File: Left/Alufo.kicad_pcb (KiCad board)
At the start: 2 copper layers, 139.7 x 88.9 mm, 73 parts, among them J1 USB_C_Receptacle_USB2.0_16P_2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, J3 USB_C_Receptacle_USB2.0_16P_2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, K11 PG1350, K12 PG1350, K13 PG1350, K14 PG1350, K15 PG1350, K16 PG1350, K21 PG1350, K22 PG1350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

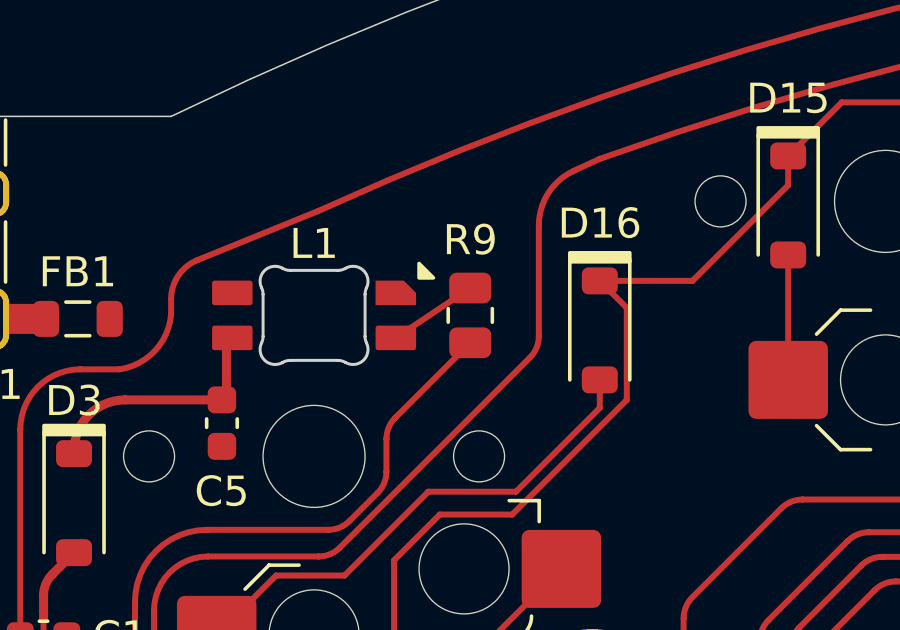
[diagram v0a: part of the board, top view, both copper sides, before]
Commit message: Remove status LED resistor
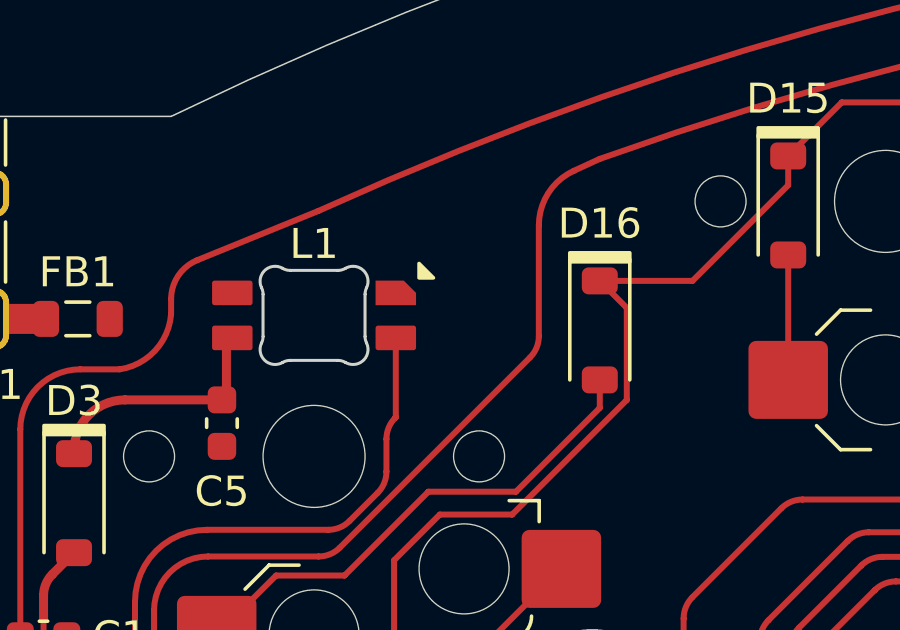
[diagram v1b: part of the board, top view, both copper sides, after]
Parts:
- removed R9: 470R, Resistor_SMD:R_0805_2012Metric
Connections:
- L1 pad 3: Net-(L1-DIN) -> LED
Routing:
- net Net-(L1-DIN): track 2.99 -> 0.00 mm
- net LED: track 25.2 -> 24.3 mm

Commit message: Update logo and add to PCB
Logo now has PCB revision included and is positioned at top left/right edge ±1.25,+1.25mm.
Author is now positioned between lowest row 2 pad 2 and bottom edge, centred to logo.
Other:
- board text added: "${AUTHOR}"
- board text removed: "${PROJECTNAME} v${PCB_REVISION} • ${AUTHOR}"

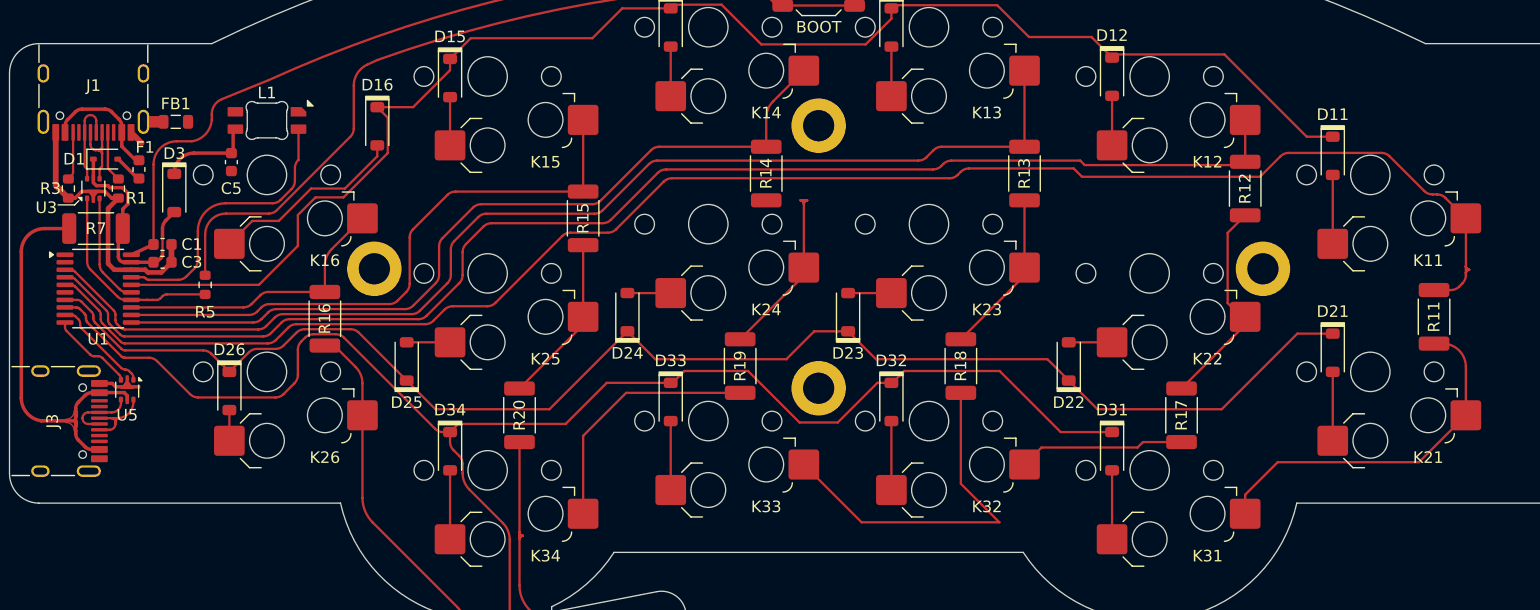
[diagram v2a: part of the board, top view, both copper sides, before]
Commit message: Align upper 0Ω resistors as on righthand, remove R11
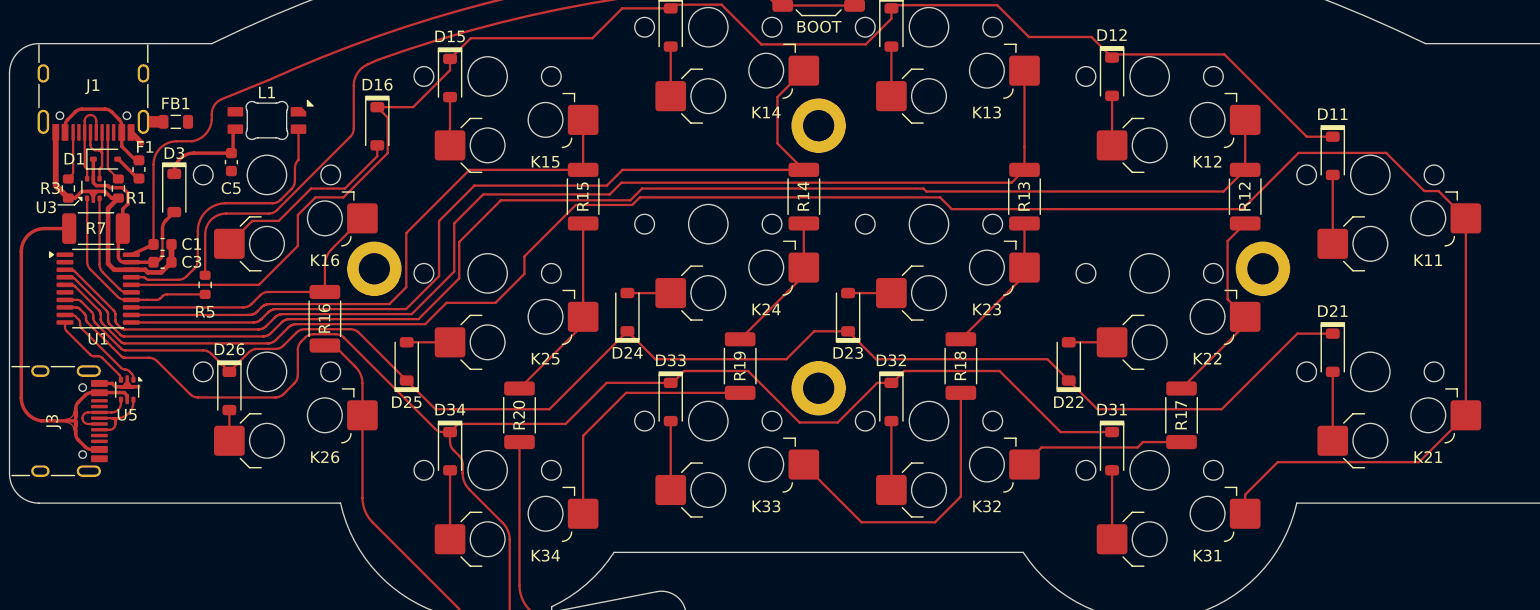
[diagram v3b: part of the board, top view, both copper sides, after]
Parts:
- removed R11: 0R, Project Library:R_2010_5025Metric_Mod
- moved R14 3.81 mm to (151.1, 54.3)
- moved R13 1.99 mm to (170.2, 54.3)
- moved R15 1.88 mm to (132.1, 54.3)
- moved R12 0.70 mm to (189.2, 54.3)
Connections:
- net Col2RT renamed Net-(K32-Pad1)
- net Col3RT renamed Net-(K33-Pad1)
- net Col4RT renamed Net-(K34-Pad1)
- K21 pad 1: Col1T -> Col1
- K31 pad 1: Col1T -> Col1
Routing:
- net Col1: track 139.7 -> 174.2 mm
- net Col1T: track 30.8 -> 0.00 mm
- net Col4L: track 70.5 -> 76.7 mm
- net Net-(K33-Pad1): track 31.5 -> 25.5 mm
- net Col3L: track 99.3 -> 101.5 mm
- net Col3R: track 13.6 -> 11.6 mm
- net Col4R: track 13.6 -> 11.6 mm
- net Col5R: track 14.0 -> 15.8 mm
- net Col2L: track 114.8 -> 116.2 mm
- net Col2R: track 18.1 -> 17.1 mm
- net Col5L: track 52.1 -> 51.2 mm

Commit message: Route Row 2 under upper 0Ω resistors
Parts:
- moved D25 13.7 mm to (127.0, 59.3), turned to -90 degrees
- moved D22 9.98 mm to (177.7, 59.3), turned to -90 degrees
- moved D23 8.47 mm to (158.7, 56.7), turned to -90 degrees
- moved D24 8.47 mm to (139.6, 56.7), turned to -90 degrees
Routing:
- net Net-(D25-A): track 3.74 -> 8.88 mm
- net Net-(D22-A): track 3.74 -> 5.95 mm
- net Row2: track 126.7 -> 128.7 mm
- net Net-(D24-A): track 3.74 -> 4.30 mm
- net Net-(D23-A): track 3.74 -> 4.30 mm
- net Col3L: track 101.5 -> 102.0 mm

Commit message: Route Row 3 under upper 0Ω resistors
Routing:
- net Row3: track 159.5 -> 217.7 mm
- net Row2: track 128.7 -> 129.8 mm
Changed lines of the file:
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@@
 		(net 48)
 	)
+	(gr_poly
+		(pts
+			(arc
+				(start 154.178 54.91)
+				(mid 154.090132 54.697868)
+				(end 153.878 54.61)
+			)
+			(arc
+				(start 154.478 54.61)
+				(mid 154.265868 54.697868)
+				(end 154.178 54.91)
+			)
+		)
+		(stroke
+			(width 0.2)
+			(type solid)
+		)
+		(fill none)
+		(layer "F.Cu")
+		(net 61)
+	)
 	(gr_arc
 		(start 114.3 42.50001)
@@
 		(net 54)
 	)
+	(gr_poly
+		(pts
+			(arc
+				(start 134.874 55.91668)
+				(mid 134.786132 55.704548)
+				(end 134.574 55.61668)
+			)
+			(arc
+				(start 135.174 55.61668)
+				(mid 134.961868 55.704548)
+				(end 134.874 55.91668)
+			)
+		)
+		(stroke
+			(width 0.2)
+			(type solid)
+		)
+		(fill none)
+		(layer "F.Cu")
+		(net 61)
+	)
 	(gr_line
 		(start 88.5444 54.6354)
@@
 	)
 	(segment
-		(start 158.68 55.01668)
-		(end 158.93 54.76668)
-		(width 0.2)
-		(layer "F.Cu")
-		(net 7)
-	)
-	(segment
 		(start 121.45 59.963686)
 		(end 121.45 62.7)
@@
 	)
 	(segment
-		(start 158.93 54.76668)
-		(end 174.879999 54.76668)
+		(start 158.68 55.01668)
+		(end 157.76532 54.102)
 		(width 0.2)
 		(layer "F.Cu")
@@
 	)
 	(segment
-		(start 174.879999 54.76668)
-		(end 177.73 57.616681)
+		(start 129.600001 55.01668)
+		(end 139.63 55.01668)
 		(width 0.2)
 		(layer "F.Cu")
@@
 	)
 	(segment
+		(start 157.76532 54.102)
+		(end 140.54468 54.102)
+		(width 0.2)
+		(layer "F.Cu")
+		(net 7)
+	)
+	(segment
 		(start 103.21679 67.729893)
 		(end 101.53 69.416683)
@@
 	)
 	(segment
-		(start 131.250001 55.01668)
-		(end 139.63 55.01668)
-		(width 0.2)
-		(layer "F.Cu")
-		(net 7)
-	)
-	(segment
 		(start 111.76 65.736111)
 		(end 108.033103 65.736111)
@@
 	)
 	(segment
-		(start 139.88 54.76668)
-		(end 139.63 55.01668)
+		(start 158.68 55.01668)
+		(end 159.59468 54.102)
 		(width 0.2)
 		(layer "F.Cu")
@@
 	)
 	(segment
-		(start 128.650001 57.616681)
-		(end 129.328341 56.938341)
+		(start 159.59468 54.102)
+		(end 174.215319 54.102)
 		(width 0.2)
 		(layer "F.Cu")
@@
 	)
 	(segment
-		(start 129.328341 56.938341)
-		(end 131.250001 55.01668)
+		(start 127 57.616681)
+		(end 129.600001 55.01668)
 		(width 0.2)
 		(layer "F.Cu")
@@
 	)
 	(segment
-		(start 158.43 54.76668)
-		(end 139.88 54.76668)
-		(width 0.2)
-		(layer "F.Cu")
-		(net 7)
-	)
-	(segment
-		(start 127 57.616681)
-		(end 128.650001 57.616681)
+		(start 107.325996 66.029004)
+		(end 106.210893 67.144107)
 		(width 0.2)
 		(layer "F.Cu")
@@
 	)
 	(segment
-		(start 107.325996 66.029004)
-		(end 106.210893 67.144107)
+		(start 174.215319 54.102)
+		(end 177.73 57.616681)
 		(width 0.2)
 		(layer "F.Cu")
@@
 	)
 	(segment
-		(start 158.68 55.01668)
-		(end 158.43 54.76668)
+		(start 140.54468 54.102)
+		(end 139.63 55.01668)
 		(width 0.2)
 		(layer "F.Cu")
@@
 	)
 	(segment
+		(start 130.835255 55.61668)
+		(end 134.874 55.61668)
+		(width 0.2)
+		(layer "F.Cu")
+		(net 61)
+	)
+	(segment
 		(start 108.776151 66.17)
 		(end 110.713786 66.17)
@@
 	)
 	(segment
-		(start 146.304 69.342)
-		(end 150.749 73.787)
+		(start 126.238 68.072)
+		(end 126.238 63.754)
+		(width 0.2)
+		(layer "F.Cu")
+		(net 61)
+	)
+	(segment
+		(start 171.86068 54.76668)
+		(end 173.228 56.134)
+		(width 0.2)
+		(layer "F.Cu")
+		(net 61)
+	)
+	(segment
+		(start 154.178 54.61)
+		(end 154.178 65.864684)
+		(width 0.2)
+		(layer "F.Cu")
+		(net 61)
+	)
+	(segment
+		(start 128.016 58.435935)
+		(end 130.835255 55.61668)
+		(width 0.2)
+		(layer "F.Cu")
+		(net 61)
+	)
+	(segment
+		(start 156.718 54.61)
+		(end 158.242 56.134)
 		(width 0.2)
 		(layer "F.Cu")
@@
 	)
 	(segment
-		(start 150.749 73.787)
-		(end 154.051 73.787)
-		(width 0.2)
-		(layer "F.Cu")
-		(net 61)
-	)
-	(segment
 		(start 92.23001 68.097914)
 		(end 92.343687 68.163544)
@@
 	)
 	(segment
-		(start 157.471316 70.366684)
-		(end 158.68 70.366684)
+		(start 127.297995 95.289219)
+		(end 128.124195 99.539653)
 		(width 0.2)
 		(layer "F.Cu")
@@
 	)
 	(segment
-		(start 127.297995 95.289219)
-		(end 128.124195 99.539653)
+		(start 138.938 56.388)
+		(end 140.466674 56.388)
 		(width 0.2)
 		(layer "F.Cu")
@@
 	)
 	(segment
-		(start 120.58 74.616684)
-		(end 121.282684 73.914)
+		(start 159.258 56.134)
+		(end 160.62532 54.76668)
 		(width 0.2)
 		(layer "F.Cu")
@@
 	)
 	(segment
-		(start 130.556 73.914)
-		(end 134.103316 70.366684)
-		(width 0.2)
-		(layer "F.Cu")
-		(net 61)
-	)
-	(segment
 		(start 87.342 63.855)
 		(end 88.274619 63.855)
@@
 	)
 	(segment
-		(start 121.282684 73.914)
-		(end 130.556 73.914)
-		(width 0.2)
-		(layer "F.Cu")
-		(net 61)
-	)
-	(segment
 		(start 92.182554 68.052554)
 		(end 92.23001 68.097914)
@@
 	)
 	(segment
-		(start 92.536107 68.199)
-		(end 94.581786 68.199)
-		(width 0.2)
-		(layer "F.Cu")
-		(net 61)
-	)
-	(segment
-		(start 158.774158 70.366684)
-		(end 159.798842 69.342)
+		(start 154.178 65.864684)
+		(end 158.68 70.366684)
 		(width 0.2)
 		(layer "F.Cu")
@@
 	)
 	(segment
-		(start 139.83766 70.316682)
-		(end 140.812342 69.342)
+		(start 92.536107 68.199)
+		(end 94.581786 68.199)
 		(width 0.2)
 		(layer "F.Cu")
@@
 	)
 	(segment
+		(start 158.242 56.134)
+		(end 159.258 56.134)
+		(width 0.2)
+		(layer "F.Cu")
+		(net 61)
+	)
+	(segment
+		(start 154.178 54.61)
+		(end 156.718 54.61)
+		(width 0.2)
+		(layer "F.Cu")
+		(net 61)
+	)
+	(segment
 		(start 122.251787 79.579787)
 		(end 125.144214 82.472214)
@@
 	)
 	(segment
-		(start 168.021 69.342)
-		(end 173.295685 74.616685)
-		(width 0.2)
-		(layer "F.Cu")
-		(net 61)
-	)
-	(segment
 		(start 120.872893 76.168893)
 		(end 121.373107 76.669107)
@@
 	)
 	(segment
+		(start 134.874 65.610684)
+		(end 139.63 70.366684)
+		(width 0.2)
+		(layer "F.Cu")
+		(net 61)
+	)
+	(segment
 		(start 89.152515 64.657476)
 		(end 89.153744 64.711798)
@@
 	)
 	(segment
+		(start 138.16668 55.61668)
+		(end 138.938 56.388)
+		(width 0.2)
+		(layer "F.Cu")
+		(net 61)
+	)
+	(segment
+		(start 134.874 55.61668)
+		(end 134.874 65.610684)
+		(width 0.2)
+		(layer "F.Cu")
+		(net 61)
+	)
+	(segment
+		(start 128.016 61.976)
+		(end 128.016 58.435935)
+		(width 0.2)
+		(layer "F.Cu")
+		(net 61)
+	)
+	(segment
 		(start 120.58 74.616684)
 		(end 120.58 75.461786)
@@
 	)
 	(segment
-		(start 154.051 73.787)
-		(end 157.471316 70.366684)
+		(start 160.62532 54.76668)
+		(end 171.86068 54.76668)
+		(width 0.2)
+		(layer "F.Cu")
+		(net 61)
+	)
+	(segment
+		(start 120.58 73.73)
+		(end 126.238 68.072)
+		(width 0.2)
+		(layer "F.Cu")
+		(net 61)
+	)
+	(segment
+		(start 134.874 55.61668)
+		(end 138.16668 55.61668)
 		(width 0.2)
 		(layer "F.Cu")
@@
 	)
 	(segment
-		(start 159.798842 69.342)
-		(end 168.021 69.342)
+		(start 142.244674 54.61)
+		(end 154.178 54.61)
+		(width 0.2)
+		(layer "F.Cu")
+		(net 61)
+	)
+	(segment
+		(start 140.466674 56.388)
+		(end 142.244674 54.61)
 		(width 0.2)
 		(layer "F.Cu")
@@
 	)
 	(segment
-		(start 140.812342 69.342)
-		(end 146.304 69.342)
+		(start 120.58 74.616684)
+		(end 120.58 73.73)
+		(width 0.2)
+		(layer "F.Cu")
+		(net 61)
+	)
+	(segment
+		(start 173.228 56.134)
+		(end 173.228 70.114685)
 		(width 0.2)
 		(layer "F.Cu")
@@
 	)
 	(segment
-		(start 173.295685 74.616685)
-		(end 177.73 74.616685)
+		(start 126.238 63.754)
+		(end 128.016 61.976)
 		(width 0.2)
 		(layer "F.Cu")
@@
 	)
 	(segment
-		(start 134.103316 70.366684)
-		(end 139.63 70.366684)
+		(start 173.228 70.114685)
+		(end 177.73 74.616685)
 		(width 0.2)
 		(layer "F.Cu")

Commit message: Remove lower 0Ω resistors
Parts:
- removed R17, R18, R19, R20: 0R, Project Library:R_2010_5025Metric_Mod
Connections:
- K22 pad 1: Col2R -> Net-(K22-Pad1)
- K23 pad 1: Col3R -> Net-(K23-Pad1)
- K24 pad 1: Col4R -> Net-(K24-Pad1)
- K25 pad 1: Col5R -> Col5T
- K32 pad 1: Net-(K32-Pad1) -> Net-(K22-Pad1)
- K33 pad 1: Net-(K33-Pad1) -> Net-(K23-Pad1)
- K34 pad 1: Net-(K34-Pad1) -> Net-(K24-Pad1)
- R12 pad 2: Col2R -> Net-(K22-Pad1)
- R13 pad 2: Col3R -> Net-(K23-Pad1)
- R14 pad 2: Col4R -> Net-(K24-Pad1)
- R15 pad 2: Col5R -> Col5T
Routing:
- net Net-(K24-Pad1): track 0.00 -> 35.3 mm
- net Net-(K22-Pad1): track 0.00 -> 33.4 mm
- net Net-(K23-Pad1): track 0.00 -> 29.3 mm
- net Net-(K33-Pad1): track 25.5 -> 0.00 mm
- net Net-(K34-Pad1): track 21.8 -> 0.00 mm
- net Col5T: track 33.6 -> 54.1 mm
- net Col2R: track 17.1 -> 0.00 mm
- net Col5R: track 15.8 -> 0.00 mm
- net Net-(K32-Pad1): track 14.4 -> 0.00 mm
- net Col4R: track 11.6 -> 0.00 mm
- net Col3R: track 11.6 -> 0.00 mm
